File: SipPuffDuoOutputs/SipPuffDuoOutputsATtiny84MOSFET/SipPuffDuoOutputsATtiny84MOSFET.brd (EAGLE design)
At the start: 48 x 70 mm, 19 parts, among them U1 ATTINY84-20PU, U2 4936BM08A-M, U3 4936BM08A-M

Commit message: .
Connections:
- net 5V: no longer L_R.2, SOLO_DUO.2
- net GND: now also L_R.2, SOLO_DUO.2
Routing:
- net 5V: track 128.5 -> 115.1 mm
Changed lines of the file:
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@@
 <contactref element="U1" pad="1"/>
 <contactref element="U$1" pad="1"/>
-<contactref element="L_R" pad="2"/>
-<contactref element="SOLO_DUO" pad="2"/>
 <contactref element="ON_OF" pad="2"/>
 <wire x1="7.4676" y1="33.528" x2="7.4676" y2="35" width="0.1524" layer="1"/>
@@
 <wire x1="2.5" y1="30" x2="7.4676" y2="34.9676" width="0.1524" layer="1"/>
 <wire x1="7.4676" y1="34.9676" x2="7.4676" y2="35" width="0.1524" layer="1"/>
-<wire x1="24" y1="52" x2="21.5" y2="54.5" width="0.1524" layer="16"/>
 <wire x1="7.43" y1="54.5" x2="3.5" y2="50.57" width="0.1524" layer="16"/>
 <wire x1="21.5" y1="54.5" x2="7.43" y2="54.5" width="0.1524" layer="16"/>
 <wire x1="3.5" y1="50.57" x2="14.07" y2="40" width="0.1524" layer="16"/>
-<wire x1="14.07" y1="40" x2="24" y2="40" width="0.1524" layer="16"/>
 </signal>
 <signal name="N$2">
@@
 <vertex x="-1.25" y="-1.04"/>
 </polygon>
+<contactref element="SOLO_DUO" pad="2"/>
+<contactref element="L_R" pad="2"/>
+<wire x1="34.725" y1="43.4954" x2="32.79" y2="50.84" width="0" layer="19" extent="1-1"/>
+<wire x1="37.265" y1="43.4954" x2="34.725" y2="43.4954" width="0" layer="19" extent="1-1"/>
+<wire x1="24" y1="52" x2="32.79" y2="50.84" width="0" layer="19" extent="1-1"/>
+<wire x1="25.275" y1="57.385" x2="24" y2="52" width="0" layer="19" extent="1-1"/>
+<wire x1="24" y1="40" x2="34.725" y2="43.4954" width="0" layer="19" extent="1-1"/>
+<wire x1="41.42" y1="32.64" x2="37.265" y2="43.4954" width="0" layer="19" extent="1-1"/>
+<wire x1="12.525" y1="42.9754" x2="24" y2="40" width="0" layer="19" extent="1-1"/>
+<wire x1="9.985" y1="42.9754" x2="12.525" y2="42.9754" width="0" layer="19" extent="1-1"/>
+<wire x1="5.04" y1="30" x2="9.985" y2="42.9754" width="0" layer="19" extent="1-1"/>
+<wire x1="16.51" y1="27.94" x2="5.04" y2="30" width="0" layer="19" extent="1-1"/>
+<wire x1="3.81" y1="15.367" x2="5.04" y2="30" width="0" layer="19" extent="1-1"/>
+<wire x1="7.62" y1="15.367" x2="3.81" y2="15.367" width="0" layer="19" extent="1-1"/>
+<wire x1="38.227" y1="15.24" x2="41.42" y2="32.64" width="0" layer="19" extent="1-1"/>
+<wire x1="32.382" y1="7.27" x2="38.227" y2="15.24" width="0" layer="19" extent="1-1"/>
 </signal>
 <signal name="N$13">

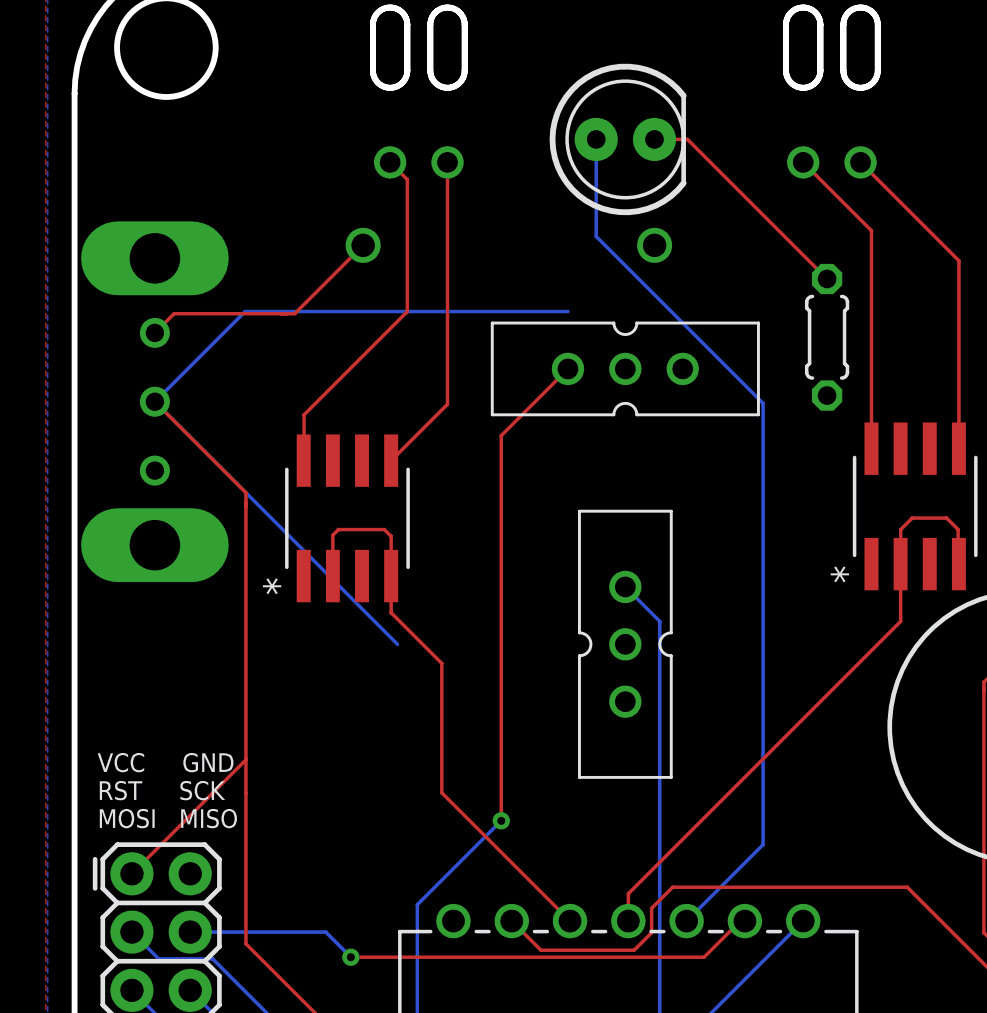
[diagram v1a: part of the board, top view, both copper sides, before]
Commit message: Changed resistors size
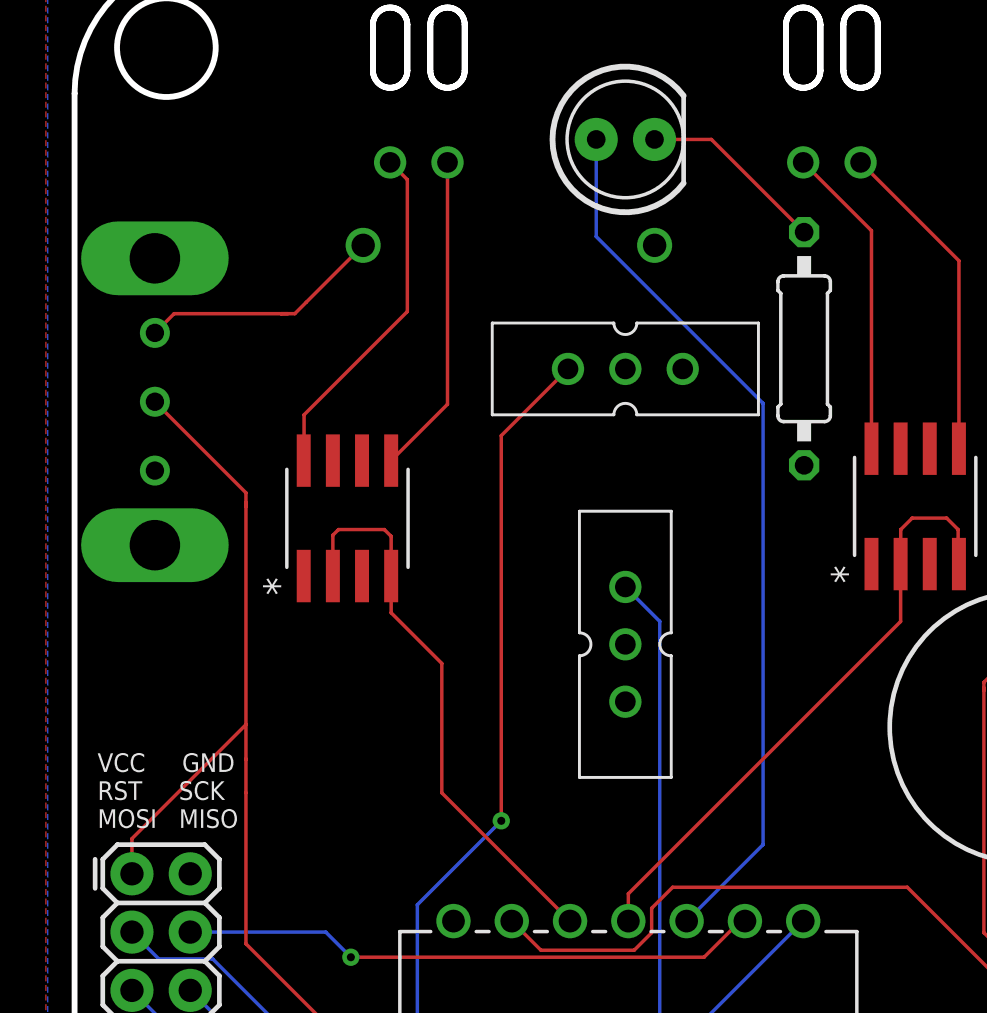
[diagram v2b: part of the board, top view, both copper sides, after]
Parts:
- R1: device MMC Eagle:RESISTOR_0204/5 -> MMC Eagle:RESISTOR_0207/10
- moved R1 1.12 mm to (31.8, 52.9)
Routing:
- net 5V: track 115.1 -> 82.0 mm
- net N$7: track 10.0 -> 8.19 mm
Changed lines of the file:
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@@
 <attribute name="VALUE" x="20.444" y="14.89" size="1.27" layer="27"/>
 </element>
-<element name="R1" library="MMC Eagle" library_urn="urn:adsk.eagle:library:3491419" package="RESISTOR_0204/5" package3d_urn="urn:adsk.eagle:package:3491543/2" value="1k" x="32.79" y="53.38" smashed="yes" rot="R90">
-<attribute name="VALUE" x="33.8986" y="53.7536" size="0.9906" layer="27" ratio="10" rot="R270"/>
+<element name="R1" library="MMC Eagle" library_urn="urn:adsk.eagle:library:3491419" package="RESISTOR_0207/10" package3d_urn="urn:adsk.eagle:package:5426338/2" value="1k" x="31.79" y="52.88" smashed="yes" rot="R90">
+<attribute name="VALUE" x="32.8986" y="53.2536" size="0.9906" layer="27" ratio="10" rot="R270"/>
 </element>
 <element name="U$1" library="MMC Eagle" library_urn="urn:adsk.eagle:library:3491419" package="2X3" package3d_urn="urn:adsk.eagle:package:4704386/2" value="HEADER_2X03" x="2.5" y="30" smashed="yes" rot="R270"/>
@@
 <contactref element="ON_OF" pad="2"/>
 <wire x1="7.4676" y1="33.528" x2="7.4676" y2="35" width="0.1524" layer="1"/>
-<wire x1="7.4676" y1="35" x2="7.4676" y2="46" width="0.1524" layer="1"/>
+<wire x1="7.4676" y1="35" x2="7.4676" y2="36.5" width="0.1524" layer="1"/>
+<wire x1="7.4676" y1="36.5" x2="7.4676" y2="46" width="0.1524" layer="1"/>
 <wire x1="7.4676" y1="46" x2="7.4676" y2="46.1772" width="0.1524" layer="1"/>
 <wire x1="3.5" y1="50.57" x2="7.4676" y2="46.6024" width="0.1524" layer="1"/>
@@
 <wire x1="14.732" y1="19.685" x2="7.4676" y2="26.9494" width="0.1524" layer="1"/>
 <wire x1="7.4676" y1="26.9494" x2="7.4676" y2="33.528" width="0.1524" layer="1"/>
-<wire x1="2.5" y1="30" x2="7.4676" y2="34.9676" width="0.1524" layer="1"/>
 <wire x1="7.4676" y1="34.9676" x2="7.4676" y2="35" width="0.1524" layer="1"/>
-<wire x1="7.43" y1="54.5" x2="3.5" y2="50.57" width="0.1524" layer="16"/>
-<wire x1="21.5" y1="54.5" x2="7.43" y2="54.5" width="0.1524" layer="16"/>
-<wire x1="3.5" y1="50.57" x2="14.07" y2="40" width="0.1524" layer="16"/>
+<wire x1="2.5" y1="30" x2="2.5" y2="31.5324" width="0.1524" layer="1"/>
+<wire x1="2.5" y1="31.5324" x2="7.4676" y2="36.5" width="0.1524" layer="1"/>
 </signal>
 <signal name="N$2">
@@
 <contactref element="D1" pad="K"/>
 <contactref element="R1" pad="2"/>
-<wire x1="32.79" y1="55.92" x2="26.71" y2="62" width="0.1524" layer="1"/>
-<wire x1="26.71" y1="62" x2="25.27" y2="62" width="0.1524" layer="1"/>
+<wire x1="25.27" y1="62" x2="27.75" y2="62" width="0.1524" layer="1"/>
+<wire x1="27.75" y1="62" x2="31.79" y2="57.96" width="0.1524" layer="1"/>
 </signal>
 <signal name="N$1">
@@
 <contactref element="SOLO_DUO" pad="2"/>
 <contactref element="L_R" pad="2"/>
-<wire x1="34.725" y1="43.4954" x2="32.79" y2="50.84" width="0" layer="19" extent="1-1"/>
-<wire x1="37.265" y1="43.4954" x2="34.725" y2="43.4954" width="0" layer="19" extent="1-1"/>
-<wire x1="24" y1="52" x2="32.79" y2="50.84" width="0" layer="19" extent="1-1"/>
-<wire x1="25.275" y1="57.385" x2="24" y2="52" width="0" layer="19" extent="1-1"/>
-<wire x1="24" y1="40" x2="34.725" y2="43.4954" width="0" layer="19" extent="1-1"/>
-<wire x1="41.42" y1="32.64" x2="37.265" y2="43.4954" width="0" layer="19" extent="1-1"/>
-<wire x1="12.525" y1="42.9754" x2="24" y2="40" width="0" layer="19" extent="1-1"/>
-<wire x1="9.985" y1="42.9754" x2="12.525" y2="42.9754" width="0" layer="19" extent="1-1"/>
-<wire x1="5.04" y1="30" x2="9.985" y2="42.9754" width="0" layer="19" extent="1-1"/>
-<wire x1="16.51" y1="27.94" x2="5.04" y2="30" width="0" layer="19" extent="1-1"/>
-<wire x1="3.81" y1="15.367" x2="5.04" y2="30" width="0" layer="19" extent="1-1"/>
-<wire x1="7.62" y1="15.367" x2="3.81" y2="15.367" width="0" layer="19" extent="1-1"/>
-<wire x1="38.227" y1="15.24" x2="41.42" y2="32.64" width="0" layer="19" extent="1-1"/>
-<wire x1="32.382" y1="7.27" x2="38.227" y2="15.24" width="0" layer="19" extent="1-1"/>
 </signal>
 <signal name="N$13">
